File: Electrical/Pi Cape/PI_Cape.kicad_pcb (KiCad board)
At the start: 2 copper layers, 11 parts, among them J1 Dist_Sensor, J2 Dist_Sensor, J3 Dist_Sensor, J4 Dist_Sensor, J5 Dist_Sensor, J6 Dist_Sensor, J7 Dist_Sensor, J8 Dist_Sensor, P1 Arduino_Interface, P2 5V_PWR_FROM_REGULATOR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

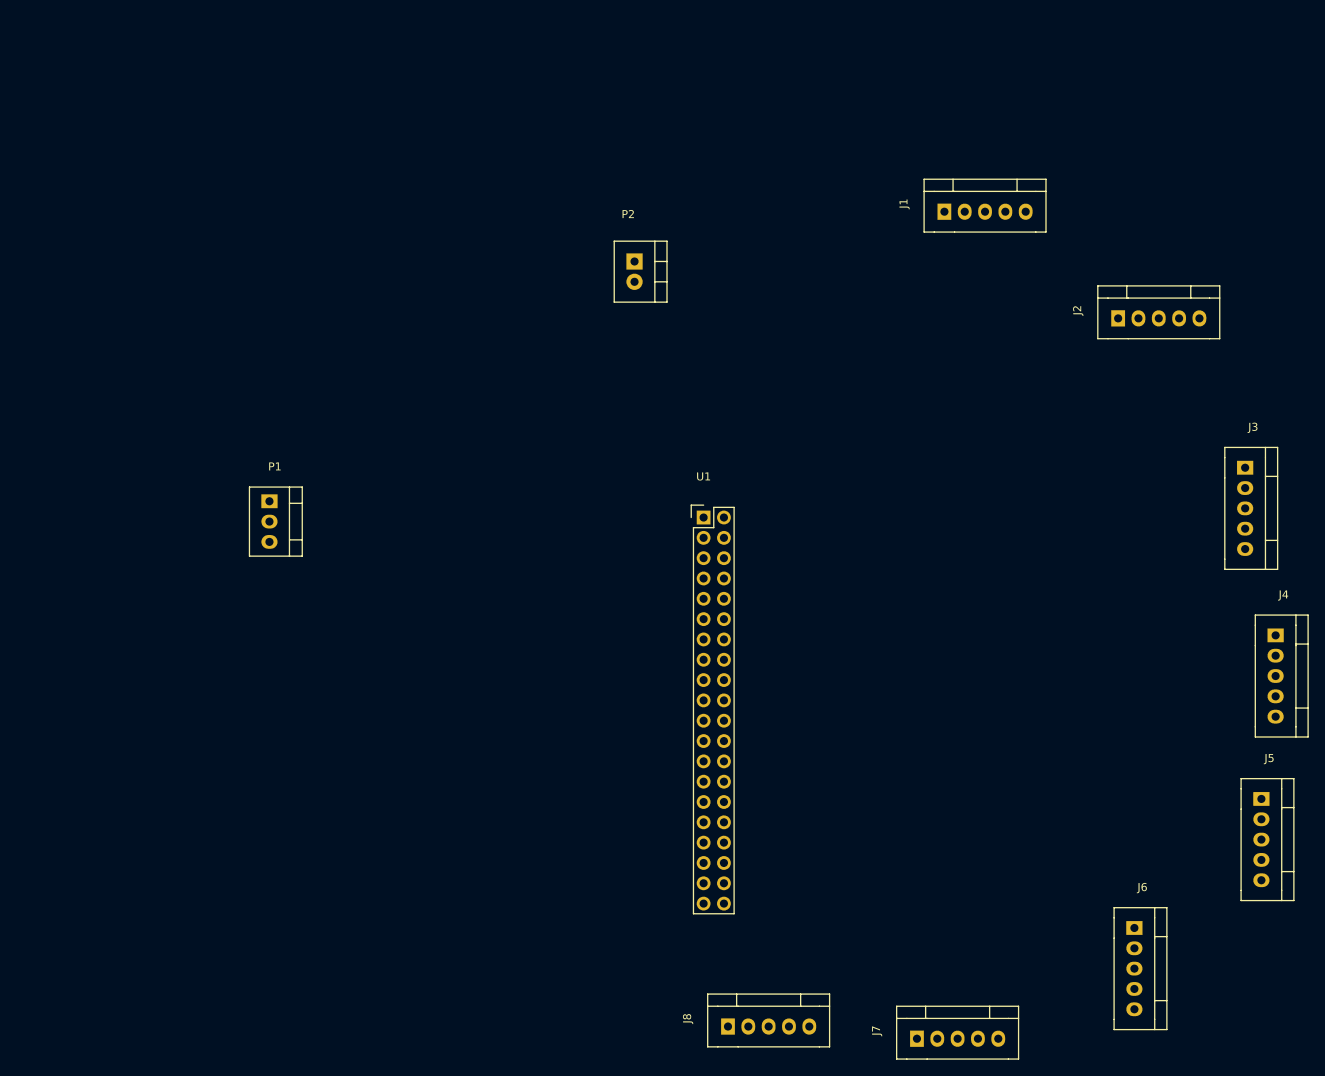
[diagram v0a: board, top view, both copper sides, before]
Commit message: updated pi cape to have 7-seg and spaced components in layout
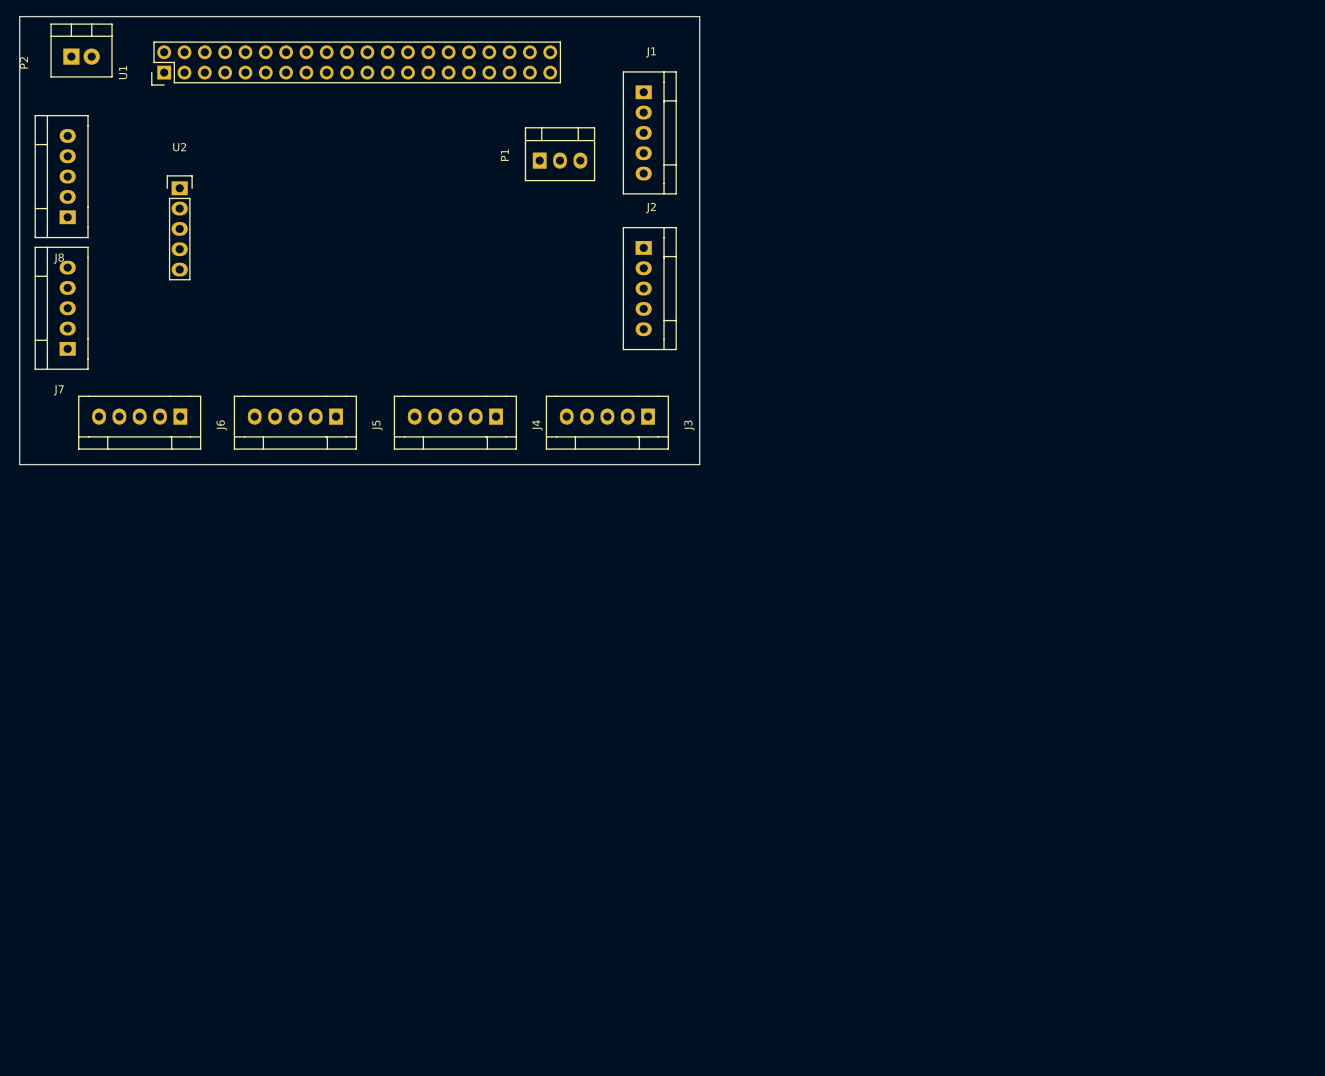
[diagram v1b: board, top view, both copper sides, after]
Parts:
- added U2: 7-segment_LED, Pin_Headers:Pin_Header_Straight_1x05, F.Cu at (45.0, 61.5)
- moved J7 132.9 mm to (33.5, 84.1), turned to 180 degrees
- moved J6 130.9 mm to (47.6, 87.5), turned to 270 degrees
- moved J8 127.4 mm to (33.5, 67.6), turned to 180 degrees
- moved J5 120.5 mm to (67.1, 87.5), turned to 270 degrees
- moved J4 96.3 mm to (87.1, 87.5), turned to 270 degrees
- moved U1 87.4 mm to (43.1, 47.0), turned to 90 degrees
- moved P2 73.3 mm to (28.9, 47.5), turned to 90 degrees
- moved J3 69.9 mm to (106.1, 87.5), turned to 270 degrees
- moved J2 60.9 mm to (100.5, 66.4), turned to 0 degrees
- moved P1 51.6 mm to (88.2, 60.5), turned to 90 degrees
- moved J1 42.6 mm to (100.5, 46.9), turned to 0 degrees
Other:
- board outline added: 85 x 56 mm
- net class Default: clearance 0.2 -> 0.1524; trace_width 0.25 -> 0.1524; via_dia 0.6 -> 0.6858; via_drill 0.4 -> 0.3302
- net class Others added: clearance 0.1524, trace_width 0.508, via_dia 0.6858, via_drill 0.3302
- net class Power added: clearance 0.1524, trace_width 1.27, via_dia 0.6858, via_drill 0.3302
- rule trace_clearance: 0.2 -> 0.1524
- rule trace_min: 0.2 -> 0.1524
- rule via_min_drill: 0.3 -> 0.3302
- rule via_min_size: 0.4 -> 0.6858

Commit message: added newest rules 3.3-1 stuff
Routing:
- net Vin: track 0.00 -> 189.6 mm, vias 0 -> 2
- net nEN_BL: track 0.00 -> 168.6 mm
- net nEN_RF: track 0.00 -> 143.7 mm, vias 0 -> 7
- net nEN_LB: track 0.00 -> 115.8 mm, vias 0 -> 5
- net I2C1_SCL: track 0.00 -> 107.3 mm, vias 0 -> 2
- net Net-(P1-Pad3): track 0.00 -> 107.1 mm, vias 0 -> 7
- net I2C0_SCL: track 0.00 -> 107.1 mm
- net nEN_LF: track 0.00 -> 105.7 mm, vias 0 -> 5
- net I2C0_SDA: track 0.00 -> 104.5 mm, vias 0 -> 2
- net I2C1_SDA: track 0.00 -> 88.9 mm, vias 0 -> 2
- net Net-(P1-Pad2): track 0.00 -> 82.2 mm, vias 0 -> 3
- net nEN_FR: track 0.00 -> 61.8 mm, vias 0 -> 7
- net nEN_FL: track 0.00 -> 56.1 mm, vias 0 -> 2
- net nEN_BR: track 0.00 -> 53.6 mm
- net 5V_PWR_IN: track 0.00 -> 41.8 mm, vias 0 -> 1
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- added copper zone on B.Cu, net GND
